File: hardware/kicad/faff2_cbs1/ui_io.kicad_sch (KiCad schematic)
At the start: 0 parts

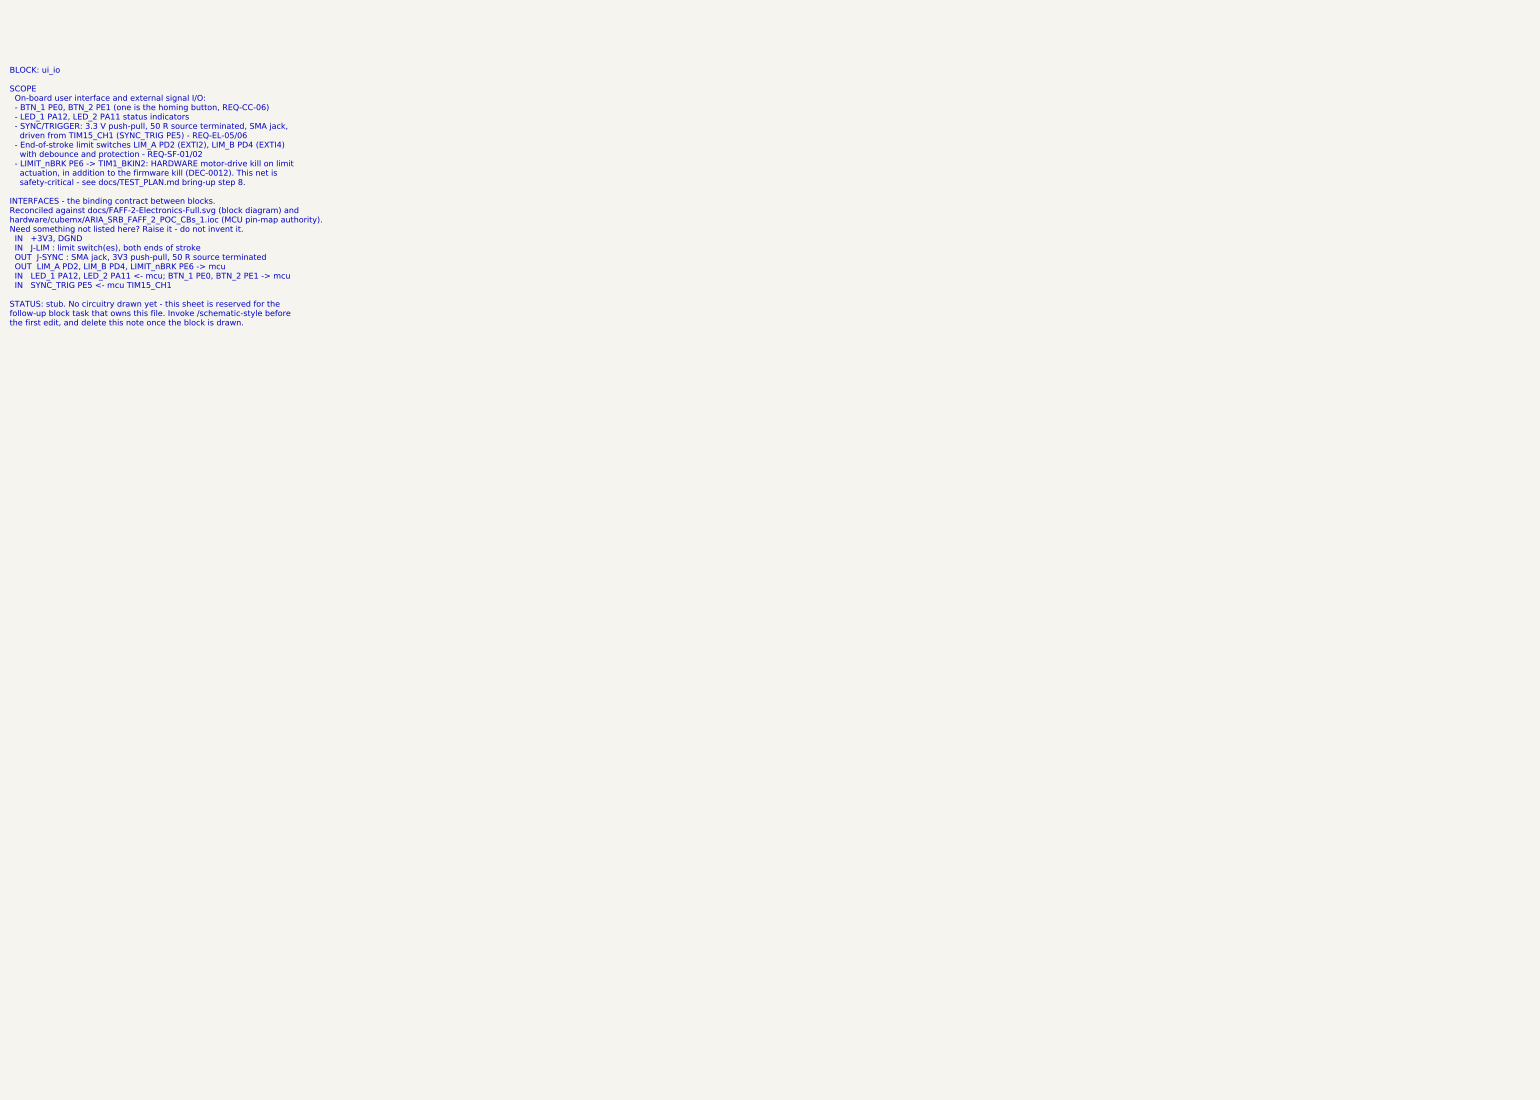
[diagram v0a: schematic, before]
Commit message: periph: draw linear_encoder, nvm_calibration and ui_io
Three peripheral block sheets for FAFF 2 CBs_1, drawn to the
/schematic-style house rules on the KiCad 9 A3 frame.

linear_encoder (REQ-PS-01..10, REQ-AR-07, DEC-0003)
  Bogen IKP11-Z1.4-P1-V5-D1-R0.5-F1000-C1 read head on two parallel
  connectors - a 10-way 0.5 mm FFC (J601, the stock Bogen cable) and a
  2x5 1.27 mm header (J602, the REQ-PS-09 alternative and the quadrature
  injection point).  AM26LV32 quad RS-422 receiver on 3V3 gives native
  3V3 outputs into TIM5; 120 R per pair, with a mid-rail reference and
  three links that switch the block to single-ended / TTL for a D3 head
  or bench injection.  Filtered 5 V read-head supply with its own
  current break, and test points on the receiver outputs.

nvm_calibration (REQ-EL-08, REQ-AR-11)
  24FC16T-I/OT 16 kbit I2C EEPROM on I2C1, 4k7 pull-ups on removable
  links, in-line solder bridges to take the device off the bus, and a
  write-protect network that resolves OQ-06 without spending an MCU pin.

ui_io (REQ-EL-05/06/09, REQ-CC-06, REQ-SF-01/02/05, DEC-0012)
  Status LEDs, two buttons with an external-button connector for the
  REQ-CC-06 homing trigger, a buffered 50 ohm source-terminated SMA
  SYNC output from TIM15_CH1, and normally-closed end-of-stroke limit
  switches whose two healthy-limit nodes are ANDed into LIMIT_nBRK for
  the TIM1_BKIN2 hardware kill.

References are allocated per sheet from the root page number (6xx, 8xx,
9xx) so the parallel block sheets cannot collide.

Datasheets fetched and committed for the parts selected here.

Co-Authored-By: Claude Opus 5 <noreply@anthropic.com>
Claude-Session: https://claude.ai/code/session_01BewsoRxMKiykAUhQw3HtBp
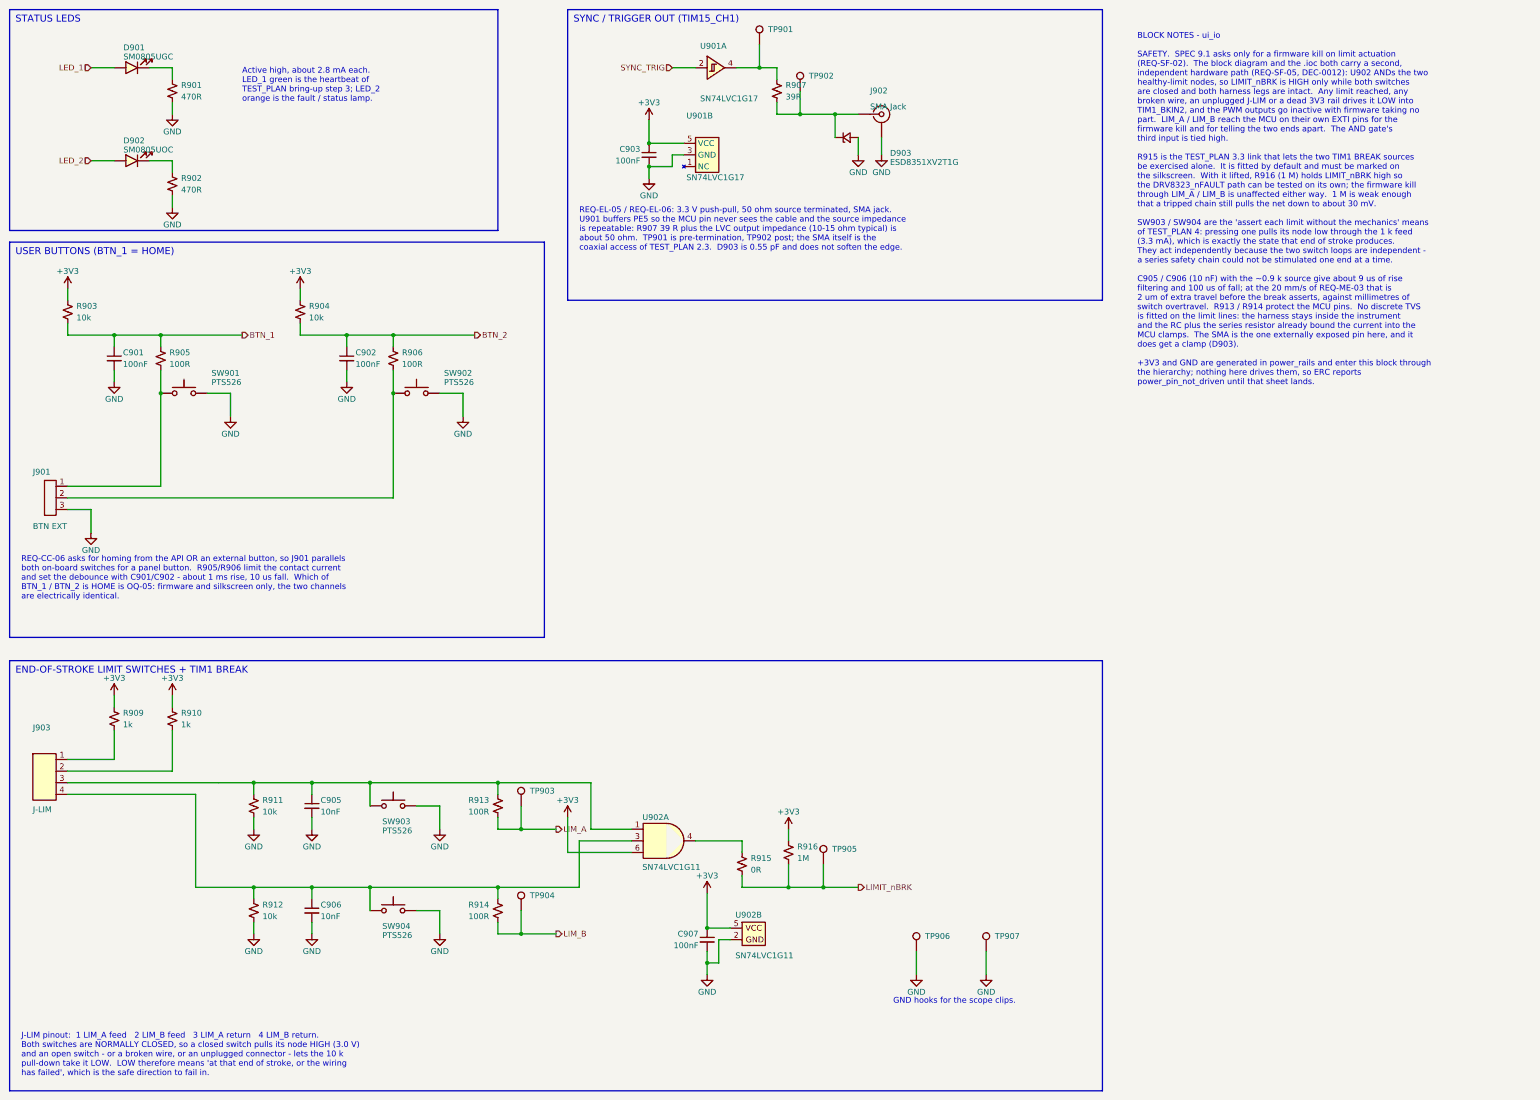
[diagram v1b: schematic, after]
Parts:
- added C901, C902, C903, C907: 100nF, Amodo:C_0603_1608Metric, symbol Amodo_Capacitors:CAP_MLCC_100nF_0603_20%_50V
- added C905, C906: 10nF, Amodo:C_0603_1608Metric, symbol Amodo_Capacitors:CAP_MLCC_10nF_0603_20%_50V
- added D901: SM0805UGC, Amodo:LED 0805 SM0805, symbol Amodo_LEDs:LED_SMD_0805_GREEN
- added D902: SM0805UOC, Amodo:LED 0805 SM0805, symbol Amodo_LEDs:LED_SMD_0805_ORANGE
- added D903: ESD8351XV2T1G, Amodo:SC-79 (SOD523), symbol Amodo_Diodes:ESD8351XV2T1G
- added J901: BTN EXT, Amodo:87224-3, symbol Amodo_Connectors:Header_Male_3-way_1-row_Straight_2.54mm_THT
- added J902: SMA Jack, Amodo:SMA-J-P-H-ST-TH1, symbol Amodo_Connectors:SMA-J-P-H-ST-TH1
- added J903: J-LIM, Amodo:B4B-XH-AM, symbol Amodo_Connectors:B4B-XH-AM
- added R901, R902: 470R, Amodo:R_0603_1608Metric, symbol Amodo_Resistors:RES_TF_470R_0603
- added R903, R904, R911, R912: 10k, Amodo:R_0603_1608Metric, symbol Amodo_Resistors:RES_TF_10k_0603
- added R905, R906, R913, R914: 100R, Amodo:R_0603_1608Metric, symbol Amodo_Resistors:RES_TF_100R_0603
- added R907: 39R, Amodo:R_0603_1608Metric, symbol Amodo_Resistors:RES_TF_39R_0603
- added R909, R910: 1k, Amodo:R_0603_1608Metric, symbol Amodo_Resistors:RES_TF_1k_0603
- added R915: 0R, Amodo:R_0603_1608Metric, symbol Amodo_Resistors:RES_TF_0R_0603
- added R916: 1M, Amodo:R_0603_1608Metric, symbol Amodo_Resistors:RES_TF_1M_0603
- added SW901, SW902, SW903, SW904: PTS526, Amodo:PTS526_1.5mm_G, symbol Amodo_Buttons:SW_TACT_5.2x5.2mm
- added TP901, TP903, TP904, TP905, TP906, TP907: TestPoint, Amodo:KeystoneMiniatureTestLoop, symbol Amodo_Connectors:TestPointHook
- added TP902: TestPoint, Amodo:TestPoint_Pad_D1.0mm, symbol Amodo_Connectors:TestPoint
- added U901: SN74LVC1G17, Amodo:SOT23-5 - TI, symbol Amodo_Digital_ICs:SN74LVC1G17
- added U902: SN74LVC1G11, Amodo:SOT23-6, symbol Amodo_Digital_ICs:SN74LVC1G11
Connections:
- new net: C906.1, J903.4, R912.1, R914.1, SW904.1_2, U902.3 (B)
- new net: D903.1 (K), J902.1 (In), R907.2, TP902.1
- new net: R907.1, TP901.1, U901.4
- new net: C905.1, J903.3, R911.1, R913.1, SW903.1_2, U902.1 (A)
- new net: R915.1, U902.4 (Y)
- new net: J901.1, R905.2, SW901.1_2
- new net: D901.2, R901.1
- new net: J901.2, R906.2, SW902.1_2
- new net: J903.2, R910.2
- new net: D902.2, R902.1
- new net: J903.1, R909.2
- new net +3V3: C903.1, C907.1, R903.1, R904.1, R909.1, R910.1, R916.1, U901.5 (VCC), U902.5 (VCC), U902.6 (C)
- new net BTN_1: C901.1, R903.2, R905.1
- new net BTN_2: C902.1, R904.2, R906.1
- new net GND: C901.2, C902.2, C903.2, C905.2, C906.2, C907.2, D903.2 (A), J901.3, J902.2 (Ext), R901.2, R902.2, R911.2, R912.2, SW901.3_4, SW902.3_4, SW903.3_4, SW904.3_4, TP906.1, TP907.1, U901.3 (GND), U902.2 (GND)
- new net LED_1: D901.1
- new net LED_2: D902.1
- new net LIMIT_nBRK: R915.2, R916.2, TP905.1
- new net LIM_A: R913.2, TP903.1
- new net LIM_B: R914.2, TP904.1
- new net SYNC_TRIG: U901.2
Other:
- note added: "Active high, about 2.8 mA each. LED_1 green is the heartbeat of TEST_PLAN bring-up step 3; LED_2 orange is the fault / status lamp."
- note added: "BLOCK NOTES - ui_io SAFETY. SPEC 9.1 asks only for a firmware kill on limit actuation (REQ-SF-02). The block diagram and the .ioc both carry a second, independent hardware path (REQ-SF-05, DEC-0012): U902 ANDs the two healthy-limit nodes, so LIMIT_nBRK is HIGH only while both switches are closed and both harness legs are intact. Any limit reached, any broken wire, an unplugged J-LIM or a dead 3V3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"
- note added: "END-OF-STROKE LIMIT SWITCHES + TIM1 BREAK"
- note added: "GND hooks for the scope clips."
- note added: "J-LIM pinout: 1 LIM_A feed 2 LIM_B feed 3 LIM_A return 4 LIM_B return. Both switches are NORMALLY CLOSED, so a closed switch pulls its node HIGH (3.0 V) and an open switch - or a broken wire, or an unplugged connector - lets the 10 k pull-down take it LOW. LOW therefore means 'at that end of stroke, or the wiring has failed', which is the safe direction to fail in."
- note added: "REQ-CC-06 asks for homing from the API OR an external button, so J901 parallels both on-board switches for a panel button. R905/R906 limit the contact current and set the debounce with C901/C902 - about 1 ms rise, 10 us fall. Which of BTN_1 / BTN_2 is HOME is OQ-05: firmware and silkscreen only, the two channels are electrically identical."
- note added: "REQ-EL-05 / REQ-EL-06: 3.3 V push-pull, 50 ohm source terminated, SMA jack. U901 buffers PE5 so the MCU pin never sees the cable and the source impedance is repeatable: R907 39 R plus the LVC output impedance (10-15 ohm typical) is about 50 ohm. TP901 is pre-termination, TP902 post; the SMA itself is the coaxial access of TEST_PLAN 2.3. D903 is 0.55 pF and does not soften the edge."
- note added: "STATUS LEDS"
- note added: "SYNC / TRIGGER OUT (TIM15_CH1)"
- note added: "USER BUTTONS (BTN_1 = HOME)"
- note removed: "BLOCK: ui_io SCOPE On-board user interface and external signal I/O: - BTN_1 PE0, BTN_2 PE1 (one is the homing button, REQ-CC-06) - LED_1 PA12, LED_2 PA11 status indicators - SYNC/TRIGGER: 3.3 V push-pull, 50 R source terminated, SMA jack, driven from TIM15_CH1 (SYNC_TRIG PE5) - REQ-EL-05/06 - End-of-stroke limit switches LIM_A PD2 (EXTI2), LIM_B PD4 (EXTI4) with debounce and protection - REQ-SF-0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"
